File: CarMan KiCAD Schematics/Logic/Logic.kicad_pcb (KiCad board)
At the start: 2 copper layers, 168.3 x 153 mm, 63 parts, among them J1 Motor Controller Can Line, J10 Motor Controller Can Line, J4 Real Time Clock, J5 Conn_02x06_Odd_Even, J7 GLV BOB, J8 PIC program, J9 IMU PS, U1 MCP9700AT-HTT-Sensor_Temperat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, U10 BNO_055, U2 ISO1050DUB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

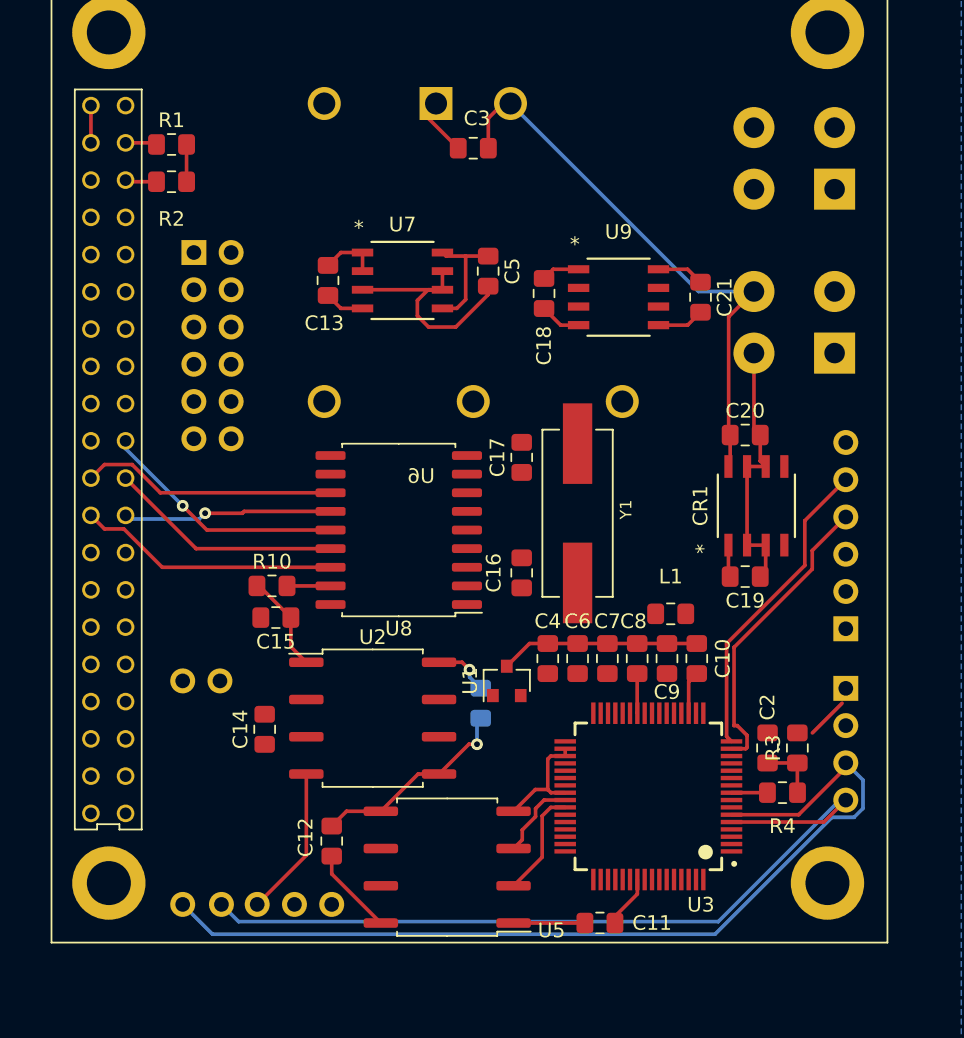
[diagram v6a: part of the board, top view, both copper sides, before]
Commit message: TSI Logic changes the 2nd
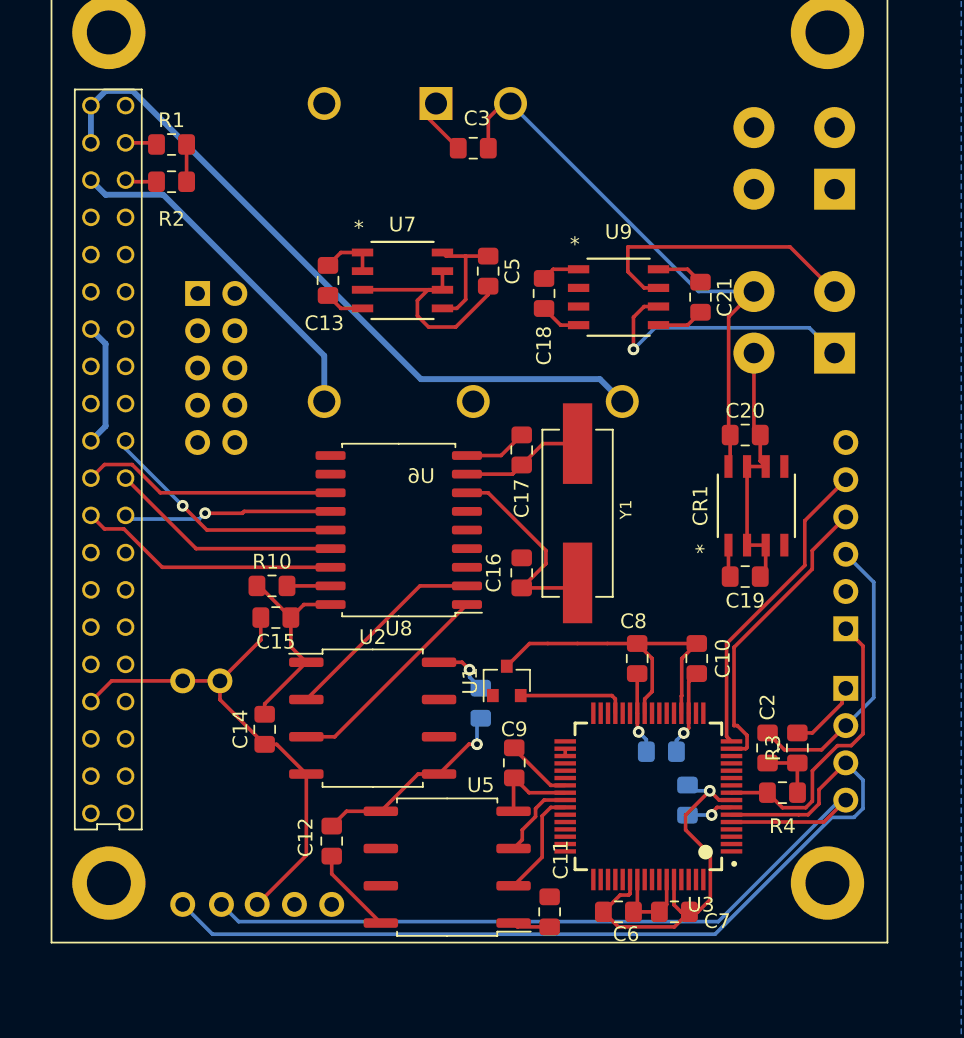
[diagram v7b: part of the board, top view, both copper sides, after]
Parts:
- removed J5: Conn_02x06_Odd_Even, Connector_PinSocket_2.54mm:PinSocket_2x06_P2.54mm_Vertical
- added J14: Conn_02x05_Odd_Even, Connector_PinSocket_2.54mm:PinSocket_2x05_P2.54mm_Vertical, B.Cu at (180.8, 71.1)
- C4, L1: moved to B.Cu
- moved C7 17.9 mm to (213.4, 113.3), turned to 0 degrees
- moved C6 17.5 mm to (209.5, 113.3), turned to 180 degrees
- moved C4 13.6 mm to (214.2, 105.7), turned to 90 degrees
- moved C9 12.6 mm to (202.4, 103.1), turned to 90 degrees
- moved L1 9.42 mm to (212.5, 102.4)
- moved C11 3.51 mm to (204.9, 113.3), turned to 90 degrees
- moved C17 0.51 mm to (202.9, 81.8), turned to 270 degrees
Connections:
- U3 pad 11: /APPS -> Net-(U3-Pad11)
- U3 pad 17: /CoolTemp -> Net-(U3-Pad17)
- U3 pad 23: /ADC_RTN -> Net-(U3-Pad23)
- U3 pad 24: /ADC_RTN -> Net-(U3-Pad24)
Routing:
- net /ISO_RTN: track 54.8 -> 150.8 mm, vias 0 -> 1
- net /5V_ISO: track 22.1 -> 73.0 mm
- net /3.3V_ISO: track 17.6 -> 57.2 mm, vias 0 -> 3
- net /SDA_TSI_GLV: track 0.00 -> 19.6 mm
- net /SCL_TSI_GLV: track 0.00 -> 19.2 mm, vias 0 -> 1
- net /~MCLR~: track 2.45 -> 20.3 mm
- net Net-(U2-Pad3): track 0.00 -> 14.7 mm
- net Net-(C16-Pad2): track 0.00 -> 14.2 mm
- net Net-(U2-Pad2): track 0.00 -> 14.2 mm
- net Net-(C17-Pad2): track 0.00 -> 8.40 mm
- net /V_OUT_TEMP: track 0.00 -> 7.52 mm
- net /SDA_ISO_PI: track 66.0 -> 66.7 mm

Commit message: Logic, TSI & GLV revisions
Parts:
- removed the J4 at (225.0, 98.0)
- removed J9: IMU PS, Connector_PinSocket_2.54mm:PinSocket_1x02_P2.54mm_Vertical
- added J6: NON-ISO CAN Testing, Connector_PinSocket_2.54mm:PinSocket_1x02_P2.54mm_Vertical, F.Cu at (156.6, 25.2)
- added U11: Raspberry_Pi_RTC, CarMan General Footprints:Raspberry_Pi_RTC, B.Cu at (224.9, 100.7)
- J2: renamed from J10; value Motor Controller Can Line -> NON-ISO I2C Testing Header
- J3: renamed from J14; value Conn_02x05_Odd_Even -> Logic-TSI Connector
- moved R7 105.6 mm to (161.2, 24.3), turned to 0 degrees
- renumbered J7 to J4, J8 to J5
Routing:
- net /3.3V_ISO: track 57.2 -> 148.5 mm, vias 3 -> 5
- net /SDA_ISO_PI: track 66.7 -> 111.2 mm
- net /SCL_ISO_PI: track 57.1 -> 100.4 mm, vias 0 -> 2
- net /ISO_RTN: track 150.8 -> 108.7 mm, vias 1 -> 7
- net /GLV_RTN: track 39.5 -> 75.4 mm
- net /SR_CTRL: track 0.00 -> 27.4 mm, vias 0 -> 2
- net /5V_ISO: track 73.0 -> 89.2 mm
- net /5V_NON_ISO: track 15.2 -> 18.4 mm
- net /SCL_TSI_GLV: track 19.2 -> 16.1 mm
- net /~MCLR~: track 20.3 -> 18.8 mm
